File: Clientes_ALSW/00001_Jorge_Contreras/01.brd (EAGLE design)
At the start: 50 x 44.9 mm, 14 parts, among them IC1 7805T

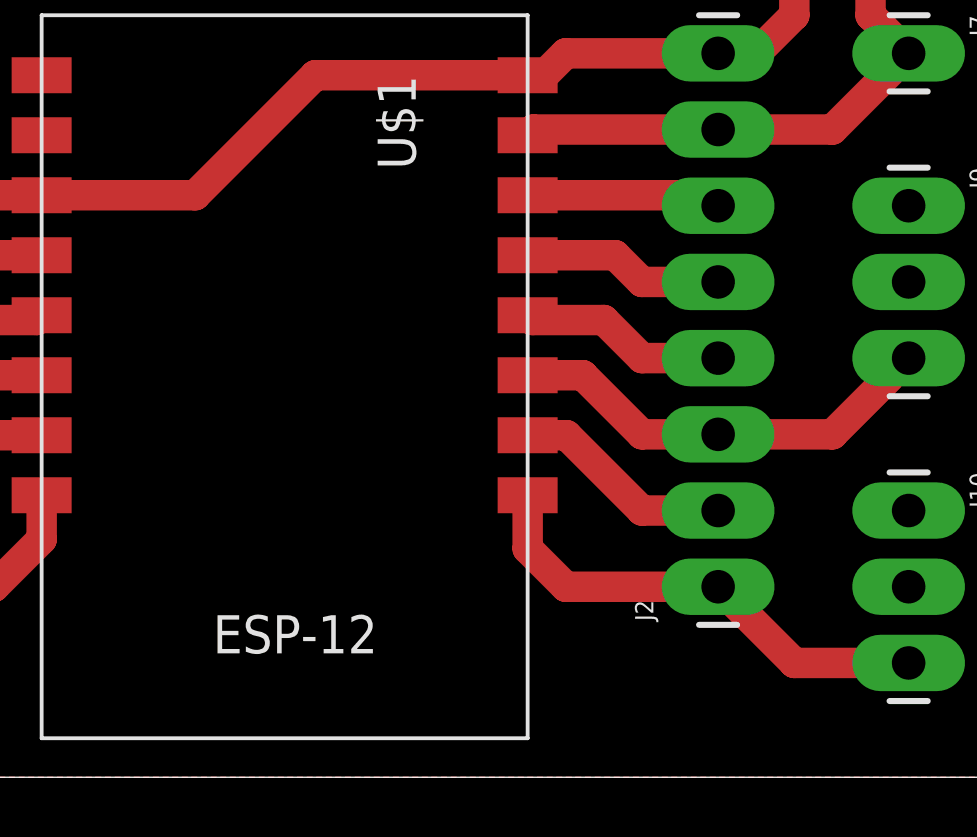
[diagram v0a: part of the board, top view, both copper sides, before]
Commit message: Correcion de pistas, generacion de pdf listos para revelar PCB
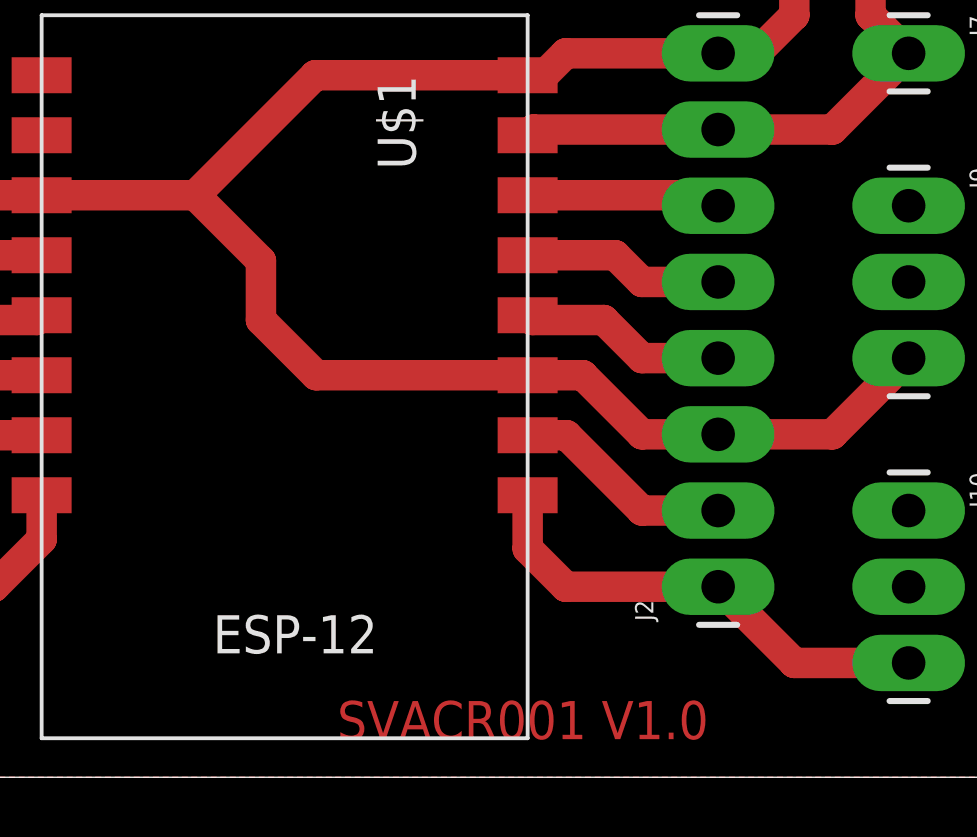
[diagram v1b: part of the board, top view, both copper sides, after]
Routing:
- net IO1: track 74.1 -> 88.8 mm
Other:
- board text added: "SVACR001 V1.0"
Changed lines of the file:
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@@
 <layer number="14" name="Route14" color="1" fill="6" visible="no" active="no"/>
 <layer number="15" name="Route15" color="4" fill="6" visible="no" active="no"/>
-<layer number="16" name="Bottom" color="1" fill="1" visible="yes" active="yes"/>
+<layer number="16" name="Bottom" color="1" fill="1" visible="no" active="yes"/>
 <layer number="17" name="Pads" color="2" fill="1" visible="yes" active="yes"/>
 <layer number="18" name="Vias" color="2" fill="1" visible="yes" active="yes"/>
 <layer number="19" name="Unrouted" color="6" fill="1" visible="yes" active="yes"/>
 <layer number="20" name="Dimension" color="24" fill="1" visible="yes" active="yes"/>
-<layer number="21" name="tPlace" color="7" fill="1" visible="yes" active="yes"/>
-<layer number="22" name="bPlace" color="7" fill="1" visible="yes" active="yes"/>
-<layer number="23" name="tOrigins" color="15" fill="1" visible="yes" active="yes"/>
-<layer number="24" name="bOrigins" color="15" fill="1" visible="yes" active="yes"/>
-<layer number="25" name="tNames" color="7" fill="1" visible="yes" active="yes"/>
-<layer number="26" name="bNames" color="7" fill="1" visible="yes" active="yes"/>
-<layer number="27" name="tValues" color="7" fill="1" visible="yes" active="yes"/>
-<layer number="28" name="bValues" color="7" fill="1" visible="yes" active="yes"/>
+<layer number="21" name="tPlace" color="7" fill="1" visible="no" active="yes"/>
+<layer number="22" name="bPlace" color="7" fill="1" visible="no" active="yes"/>
+<layer number="23" name="tOrigins" color="15" fill="1" visible="no" active="yes"/>
+<layer number="24" name="bOrigins" color="15" fill="1" visible="no" active="yes"/>
+<layer number="25" name="tNames" color="7" fill="1" visible="no" active="yes"/>
+<layer number="26" name="bNames" color="7" fill="1" visible="no" active="yes"/>
+<layer number="27" name="tValues" color="7" fill="1" visible="no" active="yes"/>
+<layer number="28" name="bValues" color="7" fill="1" visible="no" active="yes"/>
 <layer number="29" name="tStop" color="7" fill="3" visible="no" active="yes"/>
 <layer number="30" name="bStop" color="7" fill="6" visible="no" active="yes"/>
@@
 <dimension x1="0" y1="0" x2="0" y2="44.45" x3="-2.54" y3="22.225" textsize="1.778" layer="1"/>
 <dimension x1="0" y1="44.45" x2="49.53" y2="44.45" x3="24.765" y3="48.26" textsize="1.778" layer="1"/>
+<text x="26.67" y="1.27" size="1.27" layer="1" distance="30">SVACR001 V1.0</text>
 </plain>
 <attributes>
@@
 <wire x1="29.21" y1="29.21" x2="30.48" y2="27.94" width="1.016" layer="1"/>
 <wire x1="30.48" y1="27.94" x2="38.1" y2="27.94" width="1.016" layer="1"/>
-<wire x1="33.02" y1="23.4" x2="33.02" y2="13.4" width="0" layer="19" extent="1-1"/>
+<wire x1="33.02" y1="13.4" x2="25.97" y2="13.4" width="1.016" layer="1"/>
+<wire x1="24.13" y1="17.21" x2="21.94" y2="19.4" width="1.016" layer="1"/>
+<wire x1="25.97" y1="13.4" x2="24.13" y2="15.24" width="1.016" layer="1"/>
+<wire x1="24.13" y1="15.24" x2="24.13" y2="17.21" width="1.016" layer="1"/>
 </signal>
 <signal name="GPIO0">
@@
 </signal>
 </signals>
+<errors>
+</errors>
 </board>
 </drawing>
